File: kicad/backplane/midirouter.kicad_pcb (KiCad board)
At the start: 2 copper layers, 153.5 x 49 mm, 38 parts, among them J1 Conn_02x05_Odd_Even, J2 Conn_01x08, J3 Conn_01x08, J4 Conn_01x08, J5 Conn_01x08, J6 Conn_01x08, J7 Conn_01x08, J8 Conn_01x08, J9 Conn_01x08, Q1 PN2222A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

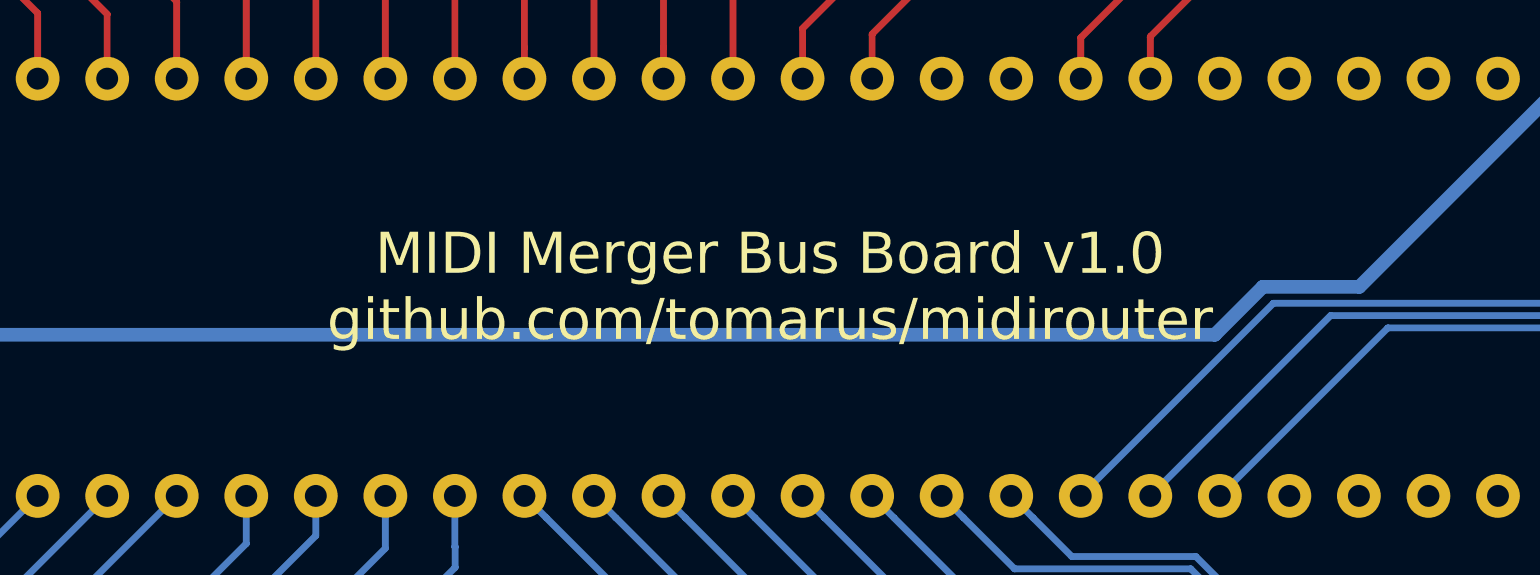
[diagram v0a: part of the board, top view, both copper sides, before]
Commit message: Silkscreen and text updates.
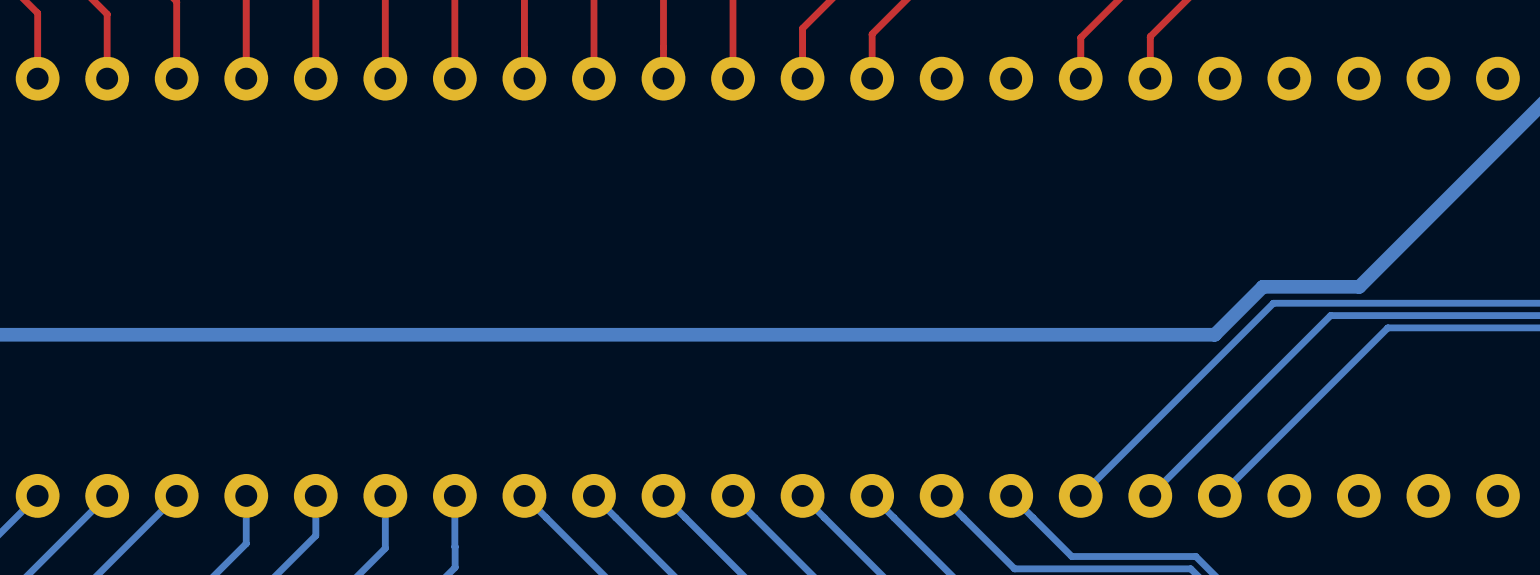
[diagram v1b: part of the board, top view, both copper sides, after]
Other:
- board text added: "MIDI ROUTER BACKPLANE V1.0 github.com/tomarus/midirouter"
- board text removed: "MIDI Merger Bus Board v1.0 github.com/tomarus/midirouter"
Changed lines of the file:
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@@
     (effects (font (size 1 1) (thickness 0.15)))
   )
-  (gr_text "MIDI Merger Bus Board v1.0\ngithub.com/tomarus/midirouter" (at 104.75 68) (layer F.SilkS)
-    (effects (font (size 1.5 1.5) (thickness 0.3)))
+  (gr_text "MIDI ROUTER\nBACKPLANE V1.0\ngithub.com/tomarus/midirouter" (at 104.75 83) (layer B.SilkS)
+    (effects (font (size 1 1) (thickness 0.15)) (justify mirror))
   )
   (dimension 153.5 (width 0.3) (layer F.Fab)
